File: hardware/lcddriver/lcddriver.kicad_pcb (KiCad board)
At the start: 2 copper layers, 75 x 40 mm, 29 parts, among them J1 Header, J2 UPDI, J3 I2C, SW1 C&K PTS526, SW2 C&K PTS526, U1 AVR32DB48, U2 LCD-S401C52TR, Y1 32.768kHz 12.5pF

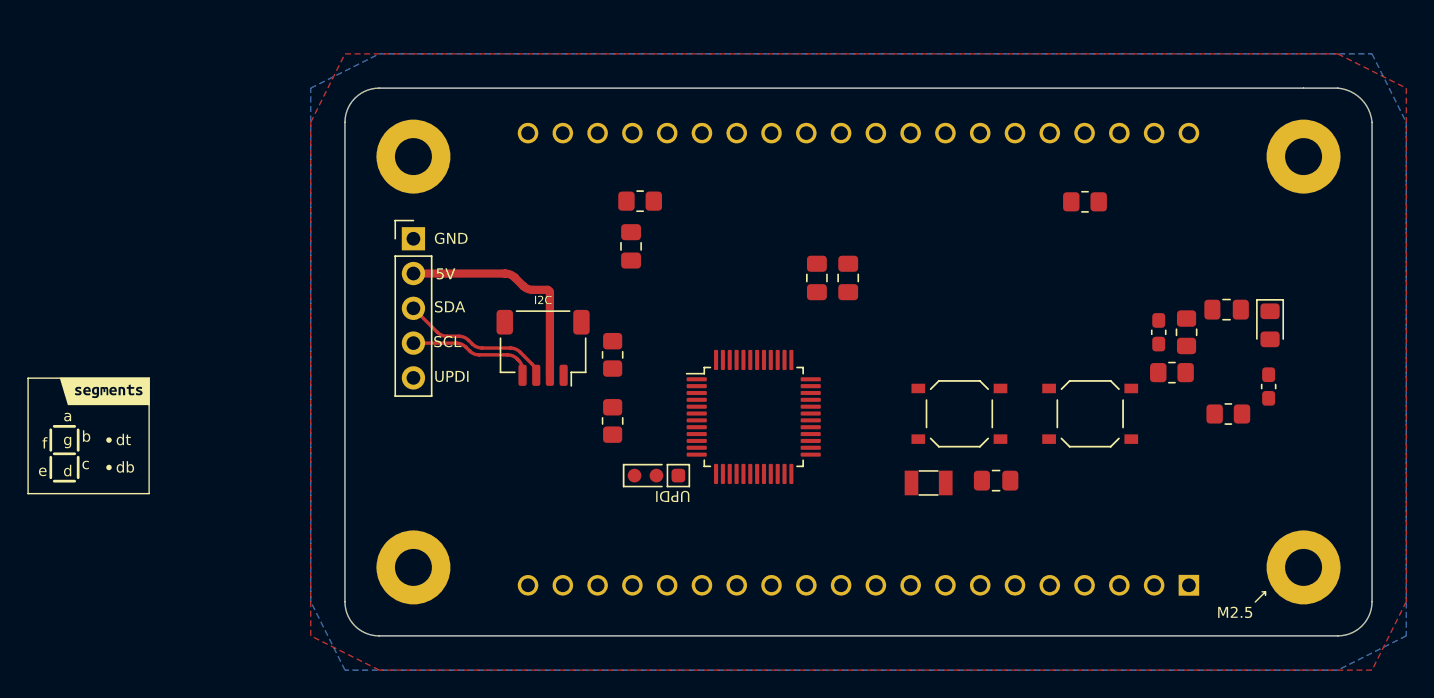
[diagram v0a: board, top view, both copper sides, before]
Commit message: hw: finished routing lcd clock face
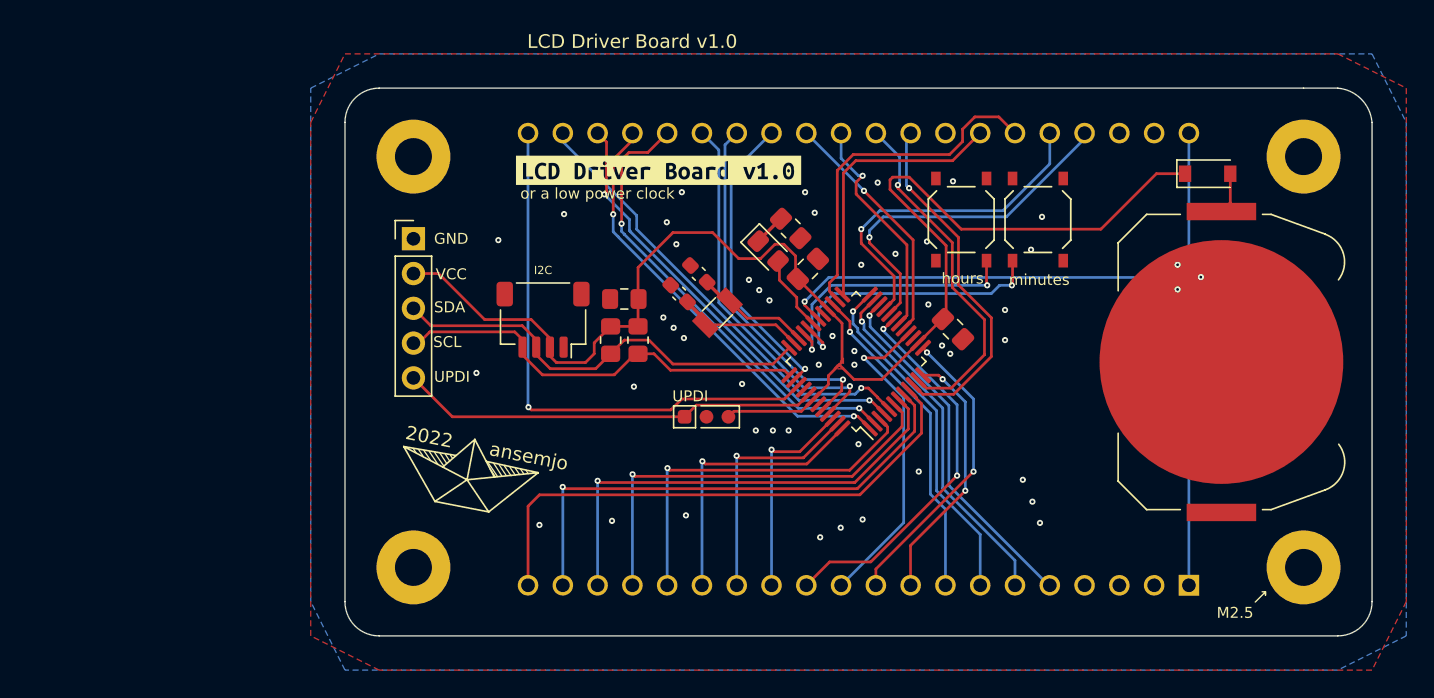
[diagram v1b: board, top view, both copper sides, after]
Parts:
- removed C6, C7: 100nF, Capacitor_SMD:C_0805_2012Metric_Pad1.18x1.45mm_HandSolder
- removed R4, R6: 10kΩ, Resistor_SMD:R_0805_2012Metric_Pad1.20x1.40mm_HandSolder
- removed R5, R7: 47kΩ, Resistor_SMD:R_0805_2012Metric_Pad1.20x1.40mm_HandSolder
- removed kibuzzard-61E3771A: G***, kibuzzard-61E3771A
- added BT1: Coin Cell, Battery:BatteryHolder_Keystone_3034_1x20mm, F.Cu at (149.0, 67.5)
- added D2: 1N5819HW, Diode_SMD:D_SOD-123, F.Cu at (148.0, 53.8)
- added kibuzzard-6311A385: G***, kibuzzard-6311A385, F.Cu at (107.9, 53.5)
- A1: footprint ansemjo:ahoi-mask -> ansemjo:ahoi
- moved R1 45.4 mm to (104.4, 65.9), turned to -90 degrees
- moved C1 43.6 mm to (109.4, 62.5), turned to 135 degrees
- moved R2 39.1 mm to (106.4, 65.9), turned to 90 degrees
- moved D1 37.1 mm to (115.9, 59.4), turned to -45 degrees
- moved C2 33.9 mm to (110.8, 61.1), turned to 135 degrees
- moved R3 29.9 mm to (117.5, 57.8), turned to -45 degrees
- moved C3 20.0 mm to (129.4, 65.1), turned to -45 degrees
- moved Y1 19.8 mm to (112.2, 63.9), turned to -135 degrees
- moved SW1 17.0 mm to (130.0, 57.1), turned to -90 degrees
- moved SW2 15.3 mm to (135.6, 57.1), turned to 90 degrees
- moved C5 14.1 mm to (105.4, 62.9), turned to 180 degrees
- moved C4 13.0 mm to (118.8, 60.7), turned to 45 degrees
- moved U1 8.50 mm to (122.3, 67.5), turned to 135 degrees
- moved J2 5.64 mm to (111.4, 71.5), turned to 0 degrees
- moved J3 2.06 mm to (99.5, 64.4)
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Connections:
- C1 pad 1: XTAL32K1 -> XTAL32K2
- C2 pad 1: XTAL32K2 -> XTAL32K1
- C3 pad 1: +5V -> VCC
- C4 pad 1: +5V -> VCC
- C5 pad 1: +5V -> VCC
- J1 pad 2: +5V -> VCC
- J2 pad 3: +5V -> VCC
- J3 pad 2: +5V -> VCC
- R1 pad 1: +5V -> VCC
- R2 pad 2: +5V -> VCC
- SW1 pad 1: VCC -> BTN2
- SW1 pad 2: Net-(R4-Pad1) -> GND
- SW2 pad 1: VCC -> BTN1
- SW2 pad 2: Net-(R6-Pad1) -> GND
- U1 pad 14: +5V -> VCC
- U1 pad 28: +5V -> VCC
- U1 pad 42: +5V -> VCC
- Y1 pad 1: XTAL32K1 -> XTAL32K2
- Y1 pad 2: XTAL32K2 -> XTAL32K1
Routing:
- net VCC: track 0.00 -> 106.0 mm
- net /COM: track 0.00 -> 63.5 mm, vias 0 -> 1
- net /4A: track 0.00 -> 40.6 mm, vias 0 -> 1
- net /4B: track 0.00 -> 40.3 mm
- net /4C: track 0.00 -> 37.7 mm, vias 0 -> 1
- net /4D: track 0.00 -> 34.4 mm, vias 0 -> 1
- net /3A: track 0.00 -> 33.7 mm, vias 0 -> 2
- net /4F: track 0.00 -> 33.5 mm, vias 0 -> 1
- net /3B: track 0.00 -> 32.5 mm, vias 0 -> 2
- net /4G: track 0.00 -> 32.4 mm, vias 0 -> 2
- net /4E: track 0.00 -> 31.2 mm, vias 0 -> 1
- net UPDI: track 0.00 -> 30.7 mm
- net /DP2: track 0.00 -> 28.4 mm, vias 0 -> 2
- net /3F: track 0.00 -> 27.8 mm, vias 0 -> 1
- net /DP3: track 0.00 -> 27.1 mm, vias 0 -> 1
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- added copper zone on B.Cu, net /COM
- added copper zone on F.Cu, net VCC
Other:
- board text added: "VCC"
- board text added: "hours"
- board text added: "minutes"
- board text added: "or a low power clock"
- board text removed: "5V"
- board text removed: "TODO: LCD Shield"
- board text removed: "a"
- board text removed: "b"
- board text removed: "c"
- board text removed: "d"
- board text removed: "db"
- board text removed: "dt"
- board text removed: "e"
- board text removed: "f"
- board text removed: "g"
